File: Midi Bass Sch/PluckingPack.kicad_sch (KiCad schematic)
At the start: 64 parts, among them Q1 BDW93C, Q2 BDW93C, Q3 BDW93C, Q4 BDW93C, Q5 BDW93C, Q6 BDW93C, Q7 BDW93C, Q8 BDW93C, Q89 BDW93C, Q90 BDW93C, Q91 BDW93C, Q92 BDW93C, U29 LTV-247, U30 LTV-247, U4 LTV-247, U5 LTV-247

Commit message: working on troubleshooting section of report
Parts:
- renumbered L92 to L10, L89 to L11, L90 to L12, L91 to L9, Q92 to Q10, Q89 to Q11, Q90 to Q12, Q91 to Q9, R304 to R46, R305 to R47, R298 to R48, R299 to R49, R306 to R50, R307 to R51, R300 to R52, R301 to R53, R308 to R54, R302 to R55, R309 to R56, R303 to R57, U30 to U6, U29 to U7

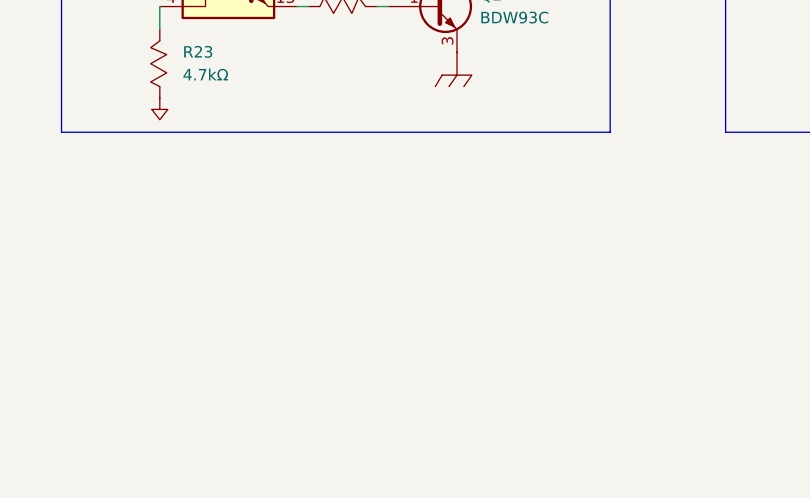
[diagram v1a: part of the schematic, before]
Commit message: working on final troubleshooting sections, modified pluck slave to header connections
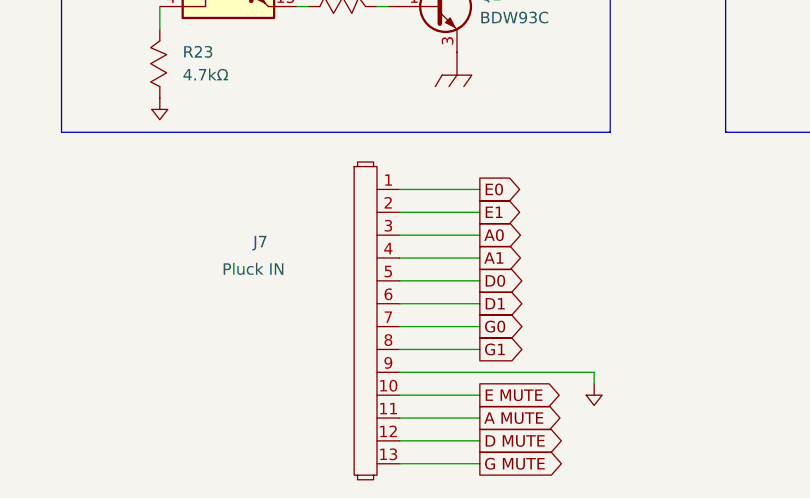
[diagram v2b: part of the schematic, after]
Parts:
- added J7: Pluck IN, symbol Owen's Symbols:Header_1x13
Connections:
- net A MUTE: now also J7.11
- net A0: now also J7.3
- net A1: now also J7.4
- net D MUTE: now also J7.12
- net D0: now also J7.5
- net D1: now also J7.6
- net E MUTE: now also J7.10
- net E0: now also J7.1
- net E1: now also J7.2
- net G MUTE: now also J7.13
- net G0: now also J7.7
- net G1: now also J7.8
- net GND: now also J7.9

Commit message: finished troubleshooting section
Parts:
- renumbered J7 to J9

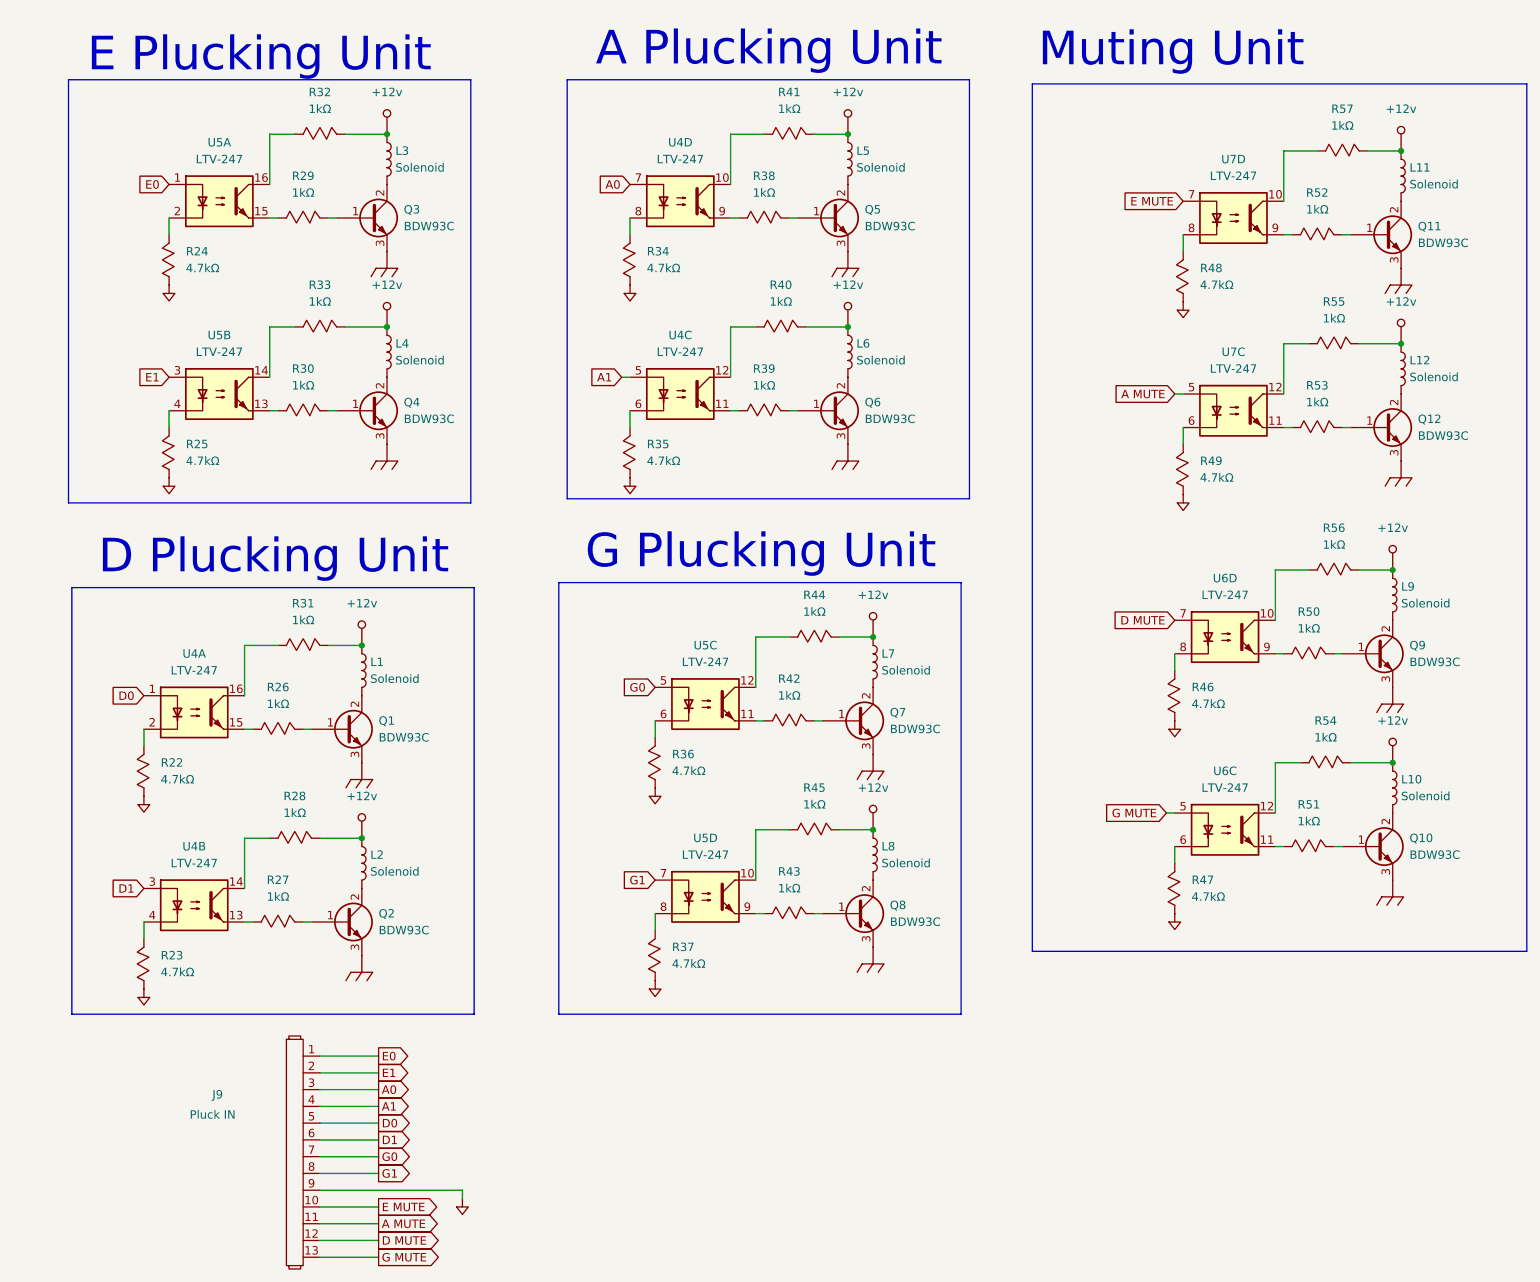
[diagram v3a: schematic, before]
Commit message: changed transistor for schematic
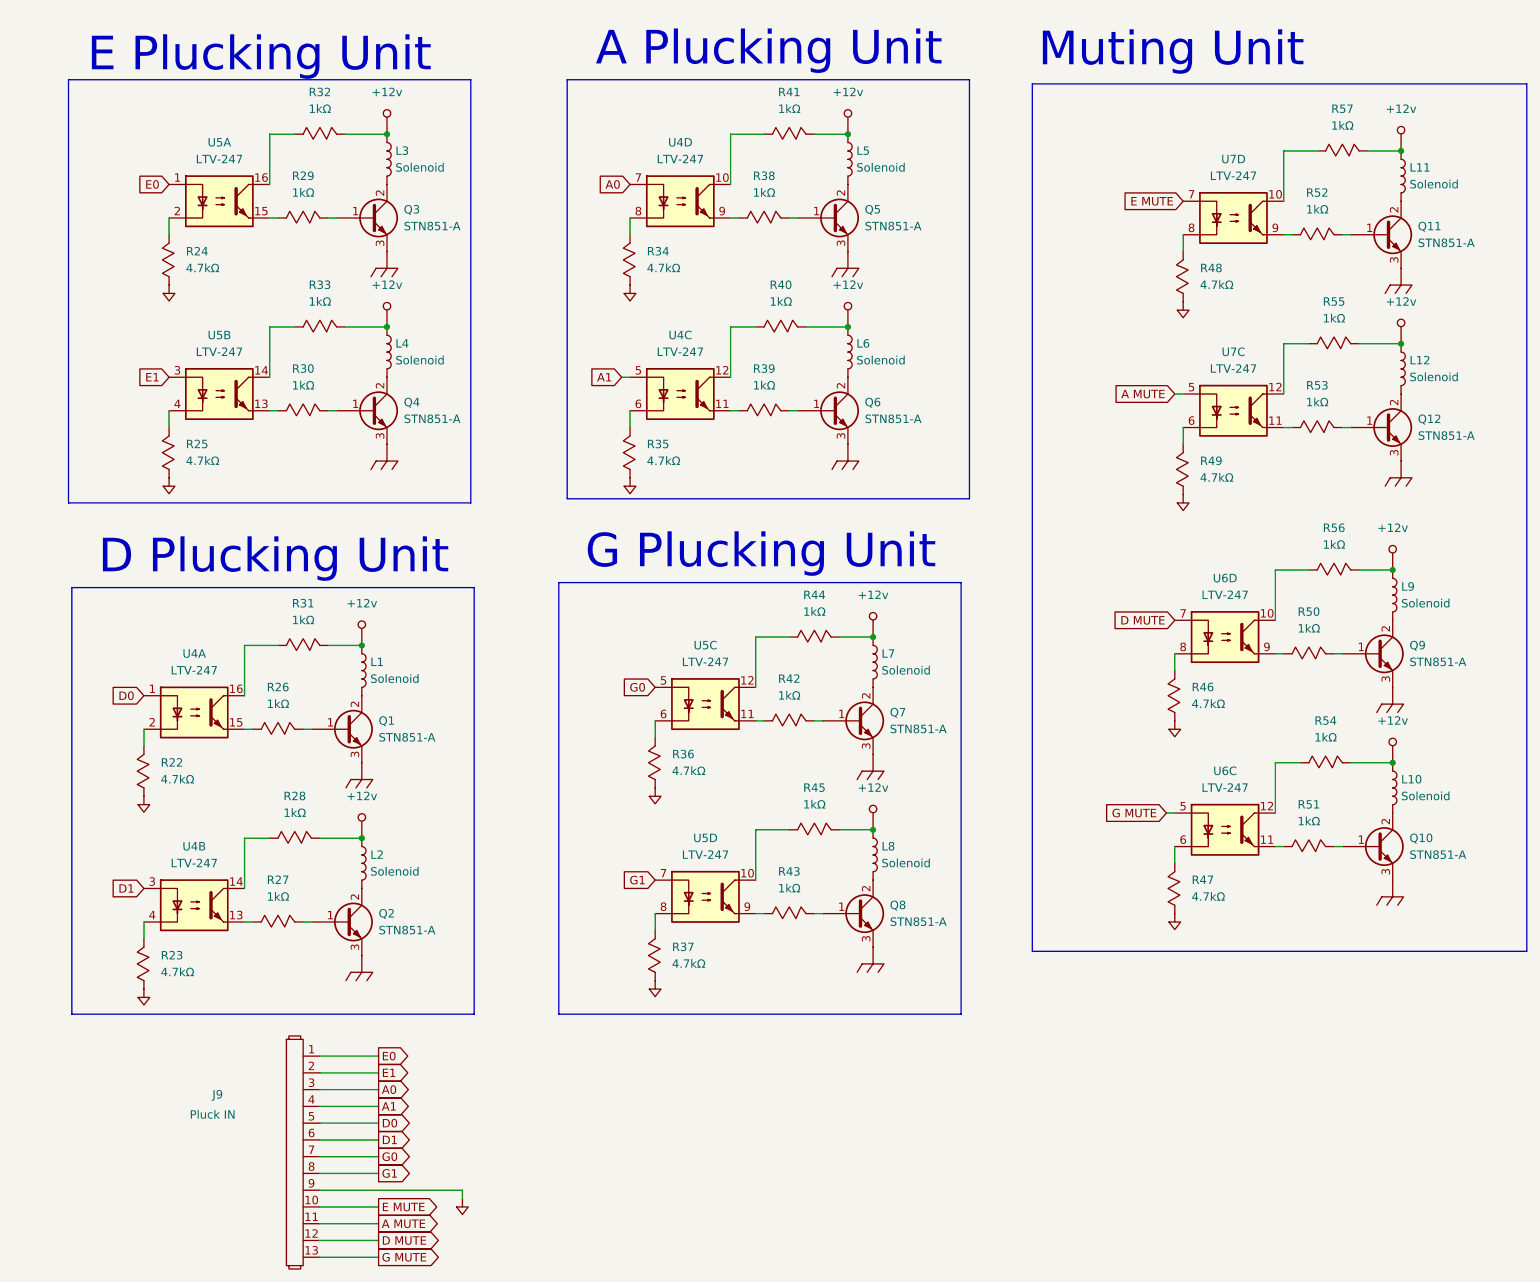
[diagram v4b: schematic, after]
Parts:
- Q1, Q10, Q11, Q12, Q2, Q3, Q4, Q5, Q6, Q7, Q8, Q9: value BDW93C -> STN851-A
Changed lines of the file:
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@@
 			)
 		)
-		(property "Value" "BDW93C"
+		(property "Value" "STN851-A"
 			(at 223.52 110.4899 0)
 			(effects
@@
 			)
 		)
-		(property "Value" "BDW93C"
+		(property "Value" "STN851-A"
 			(at 140.97 73.6599 0)
 			(effects
@@
 			)
 		)
-		(property "Value" "BDW93C"
+		(property "Value" "STN851-A"
 			(at 67.31 121.9199 0)
 			(effects
@@
 			)
 		)
-		(property "Value" "BDW93C"
+		(property "Value" "STN851-A"
 			(at 224.79 46.9899 0)
 			(effects
@@
 			)
 		)
-		(property "Value" "BDW93C"
+		(property "Value" "STN851-A"
 			(at 144.78 149.8599 0)
 			(effects
@@
 			)
 		)
-		(property "Value" "BDW93C"
+		(property "Value" "STN851-A"
 			(at 71.12 73.6599 0)
 			(effects
@@
 			)
 		)
-		(property "Value" "BDW93C"
+		(property "Value" "STN851-A"
 			(at 223.52 139.6999 0)
 			(effects
@@
 			)
 		)
-		(property "Value" "BDW93C"
+		(property "Value" "STN851-A"
 			(at 67.31 151.1299 0)
 			(effects
@@
 			)
 		)
-		(property "Value" "BDW93C"
+		(property "Value" "STN851-A"
 			(at 224.79 76.1999 0)
 			(effects
@@
 			)
 		)
-		(property "Value" "BDW93C"
+		(property "Value" "STN851-A"
 			(at 71.12 44.4499 0)
 			(effects
@@
 			)
 		)
-		(property "Value" "BDW93C"
+		(property "Value" "STN851-A"
 			(at 140.97 44.4499 0)
 			(effects
@@
 			)
 		)
-		(property "Value" "BDW93C"
+		(property "Value" "STN851-A"
 			(at 144.78 120.6499 0)
 			(effects

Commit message: began getting images for schematic appendix
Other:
- title: (none) -> Plucking Unit Solenoid Array
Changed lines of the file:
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@@
 	(generator_version "8.0")
 	(paper "A")
+	(title_block
+		(title "Plucking Unit Solenoid Array")
+		(date "2024-12-10")
+		(rev "A")
+	)
 	(junction
 		(at 68.58 30.48)

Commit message: began working on pcb layout deleted extra schematics for solenoid break out board
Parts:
- J9: footprint (none) -> Connector_PinHeader_2.54mm:PinHeader_1x13_P2.54mm_Vertical
- L1, L10, L11, L12, L2, L3, L4, L5, L6, L7, L8, L9: footprint (none) -> Connector_PinHeader_2.54mm:PinHeader_1x02_P2.54mm_Vertical
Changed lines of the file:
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@@
 			)
 		)
-		(property "Footprint" ""
+		(property "Footprint" "Connector_PinHeader_2.54mm:PinHeader_1x02_P2.54mm_Vertical"
 			(at 64.77 140.97 0)
 			(effects
@@
 			)
 		)
-		(property "Footprint" ""
+		(property "Footprint" "Connector_PinHeader_2.54mm:PinHeader_1x02_P2.54mm_Vertical"
 			(at 142.24 110.49 0)
 			(effects
@@
 			)
 		)
-		(property "Footprint" ""
+		(property "Footprint" "Connector_PinHeader_2.54mm:PinHeader_1x02_P2.54mm_Vertical"
 			(at 220.98 129.54 0)
 			(effects
@@
 			)
 		)
-		(property "Footprint" ""
+		(property "Footprint" "Connector_PinHeader_2.54mm:PinHeader_1x02_P2.54mm_Vertical"
 			(at 68.58 34.29 0)
 			(effects
@@
 			)
 		)
-		(property "Footprint" ""
+		(property "Footprint" "Connector_PinHeader_2.54mm:PinHeader_1x02_P2.54mm_Vertical"
 			(at 222.25 36.83 0)
 			(effects
@@
 			)
 		)
-		(property "Footprint" ""
+		(property "Footprint" "Connector_PinHeader_2.54mm:PinHeader_1x02_P2.54mm_Vertical"
 			(at 64.77 111.76 0)
 			(effects
@@
 			)
 		)
-		(property "Footprint" ""
+		(property "Footprint" "Connector_PinHeader_2.54mm:PinHeader_1x02_P2.54mm_Vertical"
 			(at 138.43 34.29 0)
 			(effects
@@
 			)
 		)
-		(property "Footprint" ""
+		(property "Footprint" "Connector_PinHeader_2.54mm:PinHeader_1x13_P2.54mm_Vertical"
 			(at 54.61 166.37 0)
 			(effects
@@
 			)
 		)
-		(property "Footprint" ""
+		(property "Footprint" "Connector_PinHeader_2.54mm:PinHeader_1x02_P2.54mm_Vertical"
 			(at 68.58 63.5 0)
 			(effects
@@
 			)
 		)
-		(property "Footprint" ""
+		(property "Footprint" "Connector_PinHeader_2.54mm:PinHeader_1x02_P2.54mm_Vertical"
 			(at 142.24 139.7 0)
 			(effects
@@
 			)
 		)
-		(property "Footprint" ""
+		(property "Footprint" "Connector_PinHeader_2.54mm:PinHeader_1x02_P2.54mm_Vertical"
 			(at 220.98 100.33 0)
 			(effects
@@
 			)
 		)
-		(property "Footprint" ""
+		(property "Footprint" "Connector_PinHeader_2.54mm:PinHeader_1x02_P2.54mm_Vertical"
 			(at 138.43 63.5 0)
 			(effects
@@
 			)
 		)
-		(property "Footprint" ""
+		(property "Footprint" "Connector_PinHeader_2.54mm:PinHeader_1x02_P2.54mm_Vertical"
 			(at 222.25 66.04 0)
 			(effects
